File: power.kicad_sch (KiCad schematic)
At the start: 27 parts, among them P3 USB_C_Plug_USB2.0, P4 USB_C_Plug_USB2.0, SW2 SW_SPDT, U1 AMS1117-3.3

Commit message: fix at820 sym, impl audio pa
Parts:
- removed C8: 0.1uF, symbol Device:C
- removed C9: 10uF, symbol Device:C
- removed SW2: SW_SPDT, Button_Switch_SMD:Nidec_Copal_CAS-120A, symbol Switch:SW_SPDT
- added C15: 10uF, symbol Device:C
- added C16: 0.1uF, symbol Device:C
- added R21: 0R, symbol Device:R_US
- added SW3: SW_SPDT, Button_Switch_SMD:Nidec_Copal_CAS-120A, symbol Switch:SW_SPDT
- renumbered C25 to C13, C26 to C14, C11 to C17, C10 to C18, C12 to C19, C2 to C20, C13 to C21, C27 to C22, C14 to C23, C15 to C24, D3 to D1, D5 to D2, D6 to D3, P4 to P1, P3 to P2, R24 to R10, R11 to R4, R10 to R5, R20 to R6, R21 to R7, R22 to R8, R23 to R9, U1 to U3
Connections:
- net +3V3: now also SW3.3 (C)
- net AT_PMU_1V8: now also SW3.1 (A)
- net GND: now also C15.2, C16.2, R21.2
- new net AT_QSPI_VDD: C15.1, C16.1, SW3.2 (B)
- new net GNDA: R21.1

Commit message: sch features done, all drc passed
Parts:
- renumbered C13 to C15, C14 to C16, C15 to C18, C18 to C19, C16 to C20, C19 to C21, C20 to C22, C21 to C23, C22 to C24, C23 to C25, C24 to C26, R8 to R10, R9 to R11, R21 to R12, R10 to R13, R4 to R6, R5 to R7, R6 to R8, R7 to R9, SW3 to SW5
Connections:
- net at R7.2: now also P2.SH (SHIELD); no longer P2.S1 (SHIELD)
- net at R6.2: now also P1.SH (SHIELD); no longer P1.S1 (SHIELD)
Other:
- moved on the sheet: R12

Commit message: asigning footprint
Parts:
- removed P1, P2: USB_C_Plug_USB2.0, symbol Connector:USB_C_Plug_USB2.0
- added J8, J9: USB_C_Receptacle_USB2.0_16P, Connector_USB:USB_C_Receptacle_GCT_USB4105-xx-A_16P_TopMnt_Horizontal, symbol Connector:USB_C_Receptacle_USB2.0_16P
- C15, C16, C17, C18, C19, C20, C21, C22, C23, C24, C25, C26: footprint (none) -> Capacitor_SMD:C_0603_1608Metric_Pad1.08x0.95mm_HandSolder
- D1, D2: footprint Diode_SMD:D_SOD-323 -> Diode_SMD:D_SOD-323_HandSoldering
- D3: footprint (none) -> LED_SMD:LED_0603_1608Metric_Pad1.05x0.95mm_HandSolder
- FB1: value 90R/100M -> BLM18PG121SN1D; footprint (none) -> Inductor_SMD:L_0603_1608Metric_Pad1.05x0.95mm_HandSolder
- R10, R11: footprint Resistor_SMD:R_0603_1608Metric -> Resistor_SMD:R_0603_1608Metric_Pad0.98x0.95mm_HandSolder
- R12, R13, R6, R7: footprint (none) -> Resistor_SMD:R_0603_1608Metric_Pad0.98x0.95mm_HandSolder
- R8: renamed from R9; footprint Resistor_SMD:R_0603_1608Metric -> Resistor_SMD:R_0603_1608Metric_Pad0.98x0.95mm_HandSolder
- R9: renamed from R8; footprint Resistor_SMD:R_0603_1608Metric -> Resistor_SMD:R_0603_1608Metric_Pad0.98x0.95mm_HandSolder
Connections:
- net GND: now also J8.A1 (GND), J8.A12 (GND), J8.B1 (GND), J8.B12 (GND), J9.A1 (GND), J9.A12 (GND), J9.B1 (GND), J9.B12 (GND)
- net UART_USB_D+: now also J8.A6 (D+), J8.B6 (D+)
- net UART_USB_D-: now also J8.A7 (D-), J8.B7 (D-)
- net USB_D+: now also J9.A6 (D+), J9.B6 (D+)
- net USB_D-: now also J9.A7 (D-), J9.B7 (D-)
- net VBUS: now also J8.A4 (VBUS), J8.A9 (VBUS), J8.B4 (VBUS), J8.B9 (VBUS)
- net VBUS_B: now also J9.A4 (VBUS), J9.A9 (VBUS), J9.B4 (VBUS), J9.B9 (VBUS)
- net at R11.1: now also J8.A5 (CC1)
- net at R8.1: now also J8.B5 (CC2)
- net at R7.2: now also J9.SH (SHIELD)
- net at R9.1: now also J9.B5 (CC2)
- net at R10.1: now also J9.A5 (CC1)
- net at R6.2: now also J8.SH (SHIELD)
- no-connect marks 0 -> 4
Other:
- moved on the sheet: D1, R10, R9

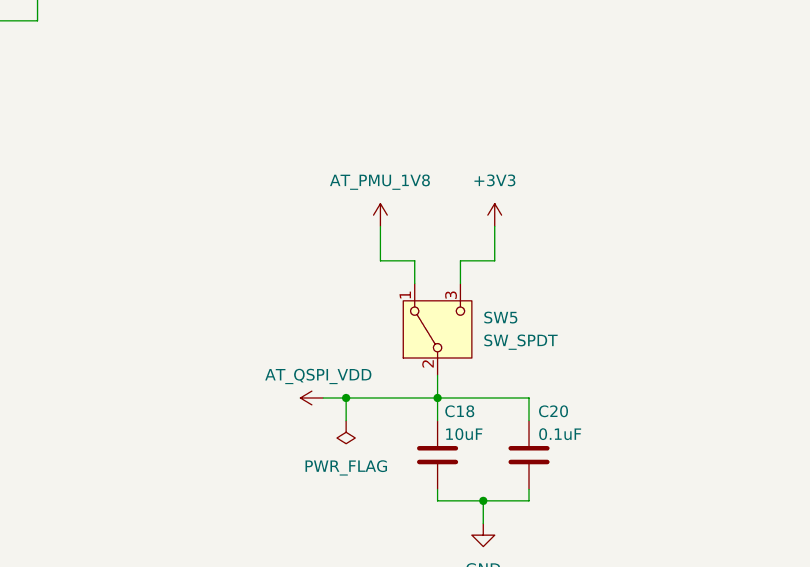
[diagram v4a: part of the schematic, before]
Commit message: refactor some switch circuit
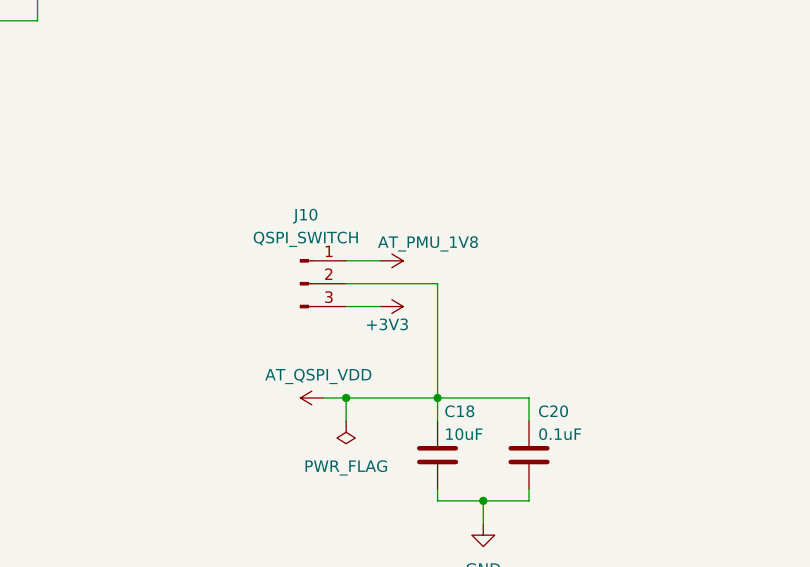
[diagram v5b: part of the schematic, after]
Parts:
- removed SW5: SW_SPDT, Button_Switch_SMD:Nidec_Copal_CAS-120A, symbol Switch:SW_SPDT
- added J10: QSPI_SWITCH, Connector_PinHeader_2.54mm:PinHeader_1x03_P2.54mm_Vertical, symbol Connector:Conn_01x03_Pin
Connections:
- net +3V3: now also J10.3 (Pin_3)
- net AT_PMU_1V8: now also J10.1 (Pin_1)
- net AT_QSPI_VDD: now also J10.2 (Pin_2)
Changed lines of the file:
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@@
 	(wire
 		(pts
-			(xy 153.67 91.44) (xy 153.67 95.25)
+			(xy 149.86 100.33) (xy 153.67 100.33)
 		)
 		(stroke
@@
 	(wire
 		(pts
-			(xy 153.67 95.25) (xy 157.48 95.25)
-		)
-		(stroke
-			(width 0)
-			(type default)
-		)
-	)
-	(wire
-		(pts
 			(xy 153.67 49.53) (xy 153.67 52.07)
 		)
@@
 	(wire
 		(pts
-			(xy 160.02 107.95) (xy 160.02 110.49)
-		)
-		(stroke
-			(width 0)
-			(type default)
-		)
-	)
-	(wire
-		(pts
 			(xy 73.66 137.16) (xy 73.66 154.94)
 		)
@@
 	(wire
 		(pts
-			(xy 157.48 95.25) (xy 157.48 97.79)
-		)
-		(stroke
-			(width 0)
-			(type default)
-		)
-	)
-	(wire
-		(pts
 			(xy 53.34 147.32) (xy 52.07 147.32)
 		)
@@
 	(wire
 		(pts
-			(xy 166.37 91.44) (xy 166.37 95.25)
-		)
-		(stroke
-			(width 0)
-			(type default)
-		)
-	)
-	(wire
-		(pts
-			(xy 166.37 95.25) (xy 162.56 95.25)
-		)
-		(stroke
-			(width 0)
-			(type default)
-		)
-	)
-	(wire
-		(pts
 			(xy 53.34 147.32) (xy 53.34 144.78)
 		)
@@
 	(wire
 		(pts
+			(xy 149.86 95.25) (xy 153.67 95.25)
+		)
+		(stroke
+			(width 0)
+			(type default)
+		)
+	)
+	(wire
+		(pts
 			(xy 194.31 52.07) (xy 194.31 49.53)
 		)
@@
 	(wire
 		(pts
-			(xy 115.57 68.58) (xy 105.41 68.58)
+			(xy 149.86 97.79) (xy 160.02 97.79)
 		)
 		(stroke
@@
 	(wire
 		(pts
-			(xy 170.18 110.49) (xy 170.18 113.03)
+			(xy 115.57 68.58) (xy 105.41 68.58)
 		)
 		(stroke
@@
 	(wire
 		(pts
-			(xy 64.77 171.45) (xy 64.77 167.64)
+			(xy 170.18 110.49) (xy 170.18 113.03)
 		)
 		(stroke
@@
 	(wire
 		(pts
-			(xy 27.94 77.47) (xy 27.94 78.74)
+			(xy 64.77 171.45) (xy 64.77 167.64)
 		)
 		(stroke
@@
 	(wire
 		(pts
-			(xy 50.8 39.37) (xy 59.69 39.37)
+			(xy 27.94 77.47) (xy 27.94 78.74)
 		)
 		(stroke
@@
 	(wire
 		(pts
-			(xy 64.77 68.58) (xy 74.93 68.58)
+			(xy 50.8 39.37) (xy 59.69 39.37)
 		)
 		(stroke
@@
 	(wire
 		(pts
-			(xy 162.56 95.25) (xy 162.56 97.79)
+			(xy 64.77 68.58) (xy 74.93 68.58)
 		)
 		(stroke
@@
 	(wire
 		(pts
+			(xy 160.02 97.79) (xy 160.02 110.49)
+		)
+		(stroke
+			(width 0)
+			(type default)
+		)
+	)
+	(wire
+		(pts
 			(xy 52.07 59.69) (xy 52.07 57.15)
 		)
@@
 	(symbol
 		(lib_id "power:+1V8")
-		(at 153.67 91.44 0)
+		(at 153.67 95.25 270)
 		(unit 1)
 		(body_style 1)
@@
 		(dnp no)
 		(property "Reference" "#PWR057"
-			(at 153.67 95.25 0)
+			(at 149.86 95.25 0)
 			(hide yes)
 			(show_name no)
@@
 		)
 		(property "Value" "AT_PMU_1V8"
-			(at 153.67 86.36 0)
+			(at 159.004 93.218 90)
 			(show_name no)
 			(do_not_autoplace no)
@@
 		)
 		(property "Footprint" ""
-			(at 153.67 91.44 0)
+			(at 153.67 95.25 0)
 			(hide yes)
 			(show_name no)
@@
 		)
 		(property "Datasheet" ""
-			(at 153.67 91.44 0)
+			(at 153.67 95.25 0)
 			(hide yes)
 			(show_name no)
@@
 		)
 		(property "Description" "Power symbol creates a global label with name \"+1V8\""
-			(at 153.67 91.44 0)
+			(at 153.67 95.25 0)
 			(hide yes)
 			(show_name no)
@@
 	)
 	(symbol
+		(lib_id "Connector:Conn_01x03_Pin")
+		(at 144.78 97.79 0)
+		(unit 1)
+		(body_style 1)
+		(exclude_from_sim no)
+		(in_bom yes)
+		(on_board yes)
+		(in_pos_files yes)
+		(dnp no)
+		(fields_autoplaced yes)
+		(property "Reference" "J10"
+			(at 145.415 90.17 0)
+			(show_name no)
+			(do_not_autoplace no)
+			(effects
+				(font
+					(size 1.27 1.27)
+				)
+			)
+		)
+		(property "Value" "QSPI_SWITCH"
+			(at 145.415 92.71 0)
+			(show_name no)
+			(do_not_autoplace no)
+			(effects
+				(font
+					(size 1.27 1.27)
+				)
+			)
+		)
+		(property "Footprint" "Connector_PinHeader_2.54mm:PinHeader_1x03_P2.54mm_Vertical"
+			(at 144.78 97.79 0)
+			(hide yes)
+			(show_name no)
+			(do_not_autoplace no)
+			(effects
+				(font
+					(size 1.27 1.27)
+				)
+			)
+		)
+		(property "Datasheet" ""
+			(at 144.78 97.79 0)
+			(hide yes)
+			(show_name no)
+			(do_not_autoplace no)
+			(effects
+				(font
+					(size 1.27 1.27)
+				)
+			)
+		)
+		(property "Description" "Generic connector, single row, 01x03, script generated"
+			(at 144.78 97.79 0)
+			(hide yes)
+			(show_name no)
+			(do_not_autoplace no)
+			(effects
+				(font
+					(size 1.27 1.27)
+				)
+			)
+		)
+		(pin "1"
+		)
+		(pin "2"
+		)
+		(pin "3"
+		)
+		(instances
+			(project "at820_picokit"
+				(path "/a8c0f85c-55b6-4da9-ba8c-71a36ed08e24/bdb32295-0012-48b2-b3aa-c4e9dc671aef"
+					(reference "J10")
+					(unit 1)
+				)
+			)
+		)
+	)
+	(symbol
 		(lib_id "Device:C")
 		(at 179.07 45.72 0)
@@
 	(symbol
 		(lib_id "power:+3V3")
-		(at 166.37 91.44 0)
+		(at 153.67 100.33 270)
 		(unit 1)
 		(body_style 1)
@@
 		(in_pos_files yes)
 		(dnp no)
-		(fields_autoplaced yes)
 		(property "Reference" "#PWR060"
-			(at 166.37 95.25 0)
+			(at 149.86 100.33 0)
 			(hide yes)
 			(show_name no)
@@
 		)
 		(property "Value" "+3V3"
-			(at 166.37 86.36 0)
+			(at 154.432 102.362 90)
 			(show_name no)
 			(do_not_autoplace no)
@@
 		)
 		(property "Footprint" ""
-			(at 166.37 91.44 0)
+			(at 153.67 100.33 0)
 			(hide yes)
 			(show_name no)
@@
 		)
 		(property "Datasheet" ""
-			(at 166.37 91.44 0)
+			(at 153.67 100.33 0)
 			(hide yes)
 			(show_name no)
@@
 		)
 		(property "Description" "Power symbol creates a global label with name \"+3V3\""
-			(at 166.37 91.44 0)
+			(at 153.67 100.33 0)
 			(hide yes)
 			(show_name no)
@@
 					(unit 1)
 				)
-			)
-		)
-	)
-	(symbol
-		(lib_id "Switch:SW_SPDT")
-		(at 160.02 102.87 90)
-		(unit 1)
-		(body_style 1)
-		(exclude_from_sim no)
-		(in_bom yes)
-		(on_board yes)
-		(in_pos_files yes)
-		(dnp no)
-		(fields_autoplaced yes)
-		(property "Reference" "SW5"
-			(at 165.1 101.5999 90)
-			(show_name no)
-			(do_not_autoplace no)
-			(effects
-				(font
-					(size 1.27 1.27)
-				)
-				(justify right)
-			)
-		)
-		(property "Value" "SW_SPDT"
-			(at 165.1 104.1399 90)
-			(show_name no)
-			(do_not_autoplace no)
-			(effects
-				(font
-					(size 1.27 1.27)
-				)
-				(justify right)
-			)
-		)
-		(property "Footprint" "Button_Switch_SMD:Nidec_Copal_CAS-120A"
-			(at 160.02 102.87 0)
-			(hide yes)
-			(show_name no)
-			(do_not_autoplace no)
-			(effects
-				(font
-					(size 1.27 1.27)
-				)
-			)
-		)
-		(property "Datasheet" ""
-			(at 167.64 102.87 0)
-			(hide yes)
-			(show_name no)
-			(do_not_autoplace no)
-			(effects
-				(font
-					(size 1.27 1.27)
-				)
-			)
-		)
-		(property "Description" "Switch, single pole double throw"
-			(at 160.02 102.87 0)
-			(hide yes)
-			(show_name no)
-			(do_not_autoplace no)
-			(effects
-				(font
-					(size 1.27 1.27)
-				)
-			)
-		)
-		(pin "3"
-		)
-		(pin "1"
-		)
-		(pin "2"
-		)
-		(instances
-			(project "at820_picokit"
-				(path "/a8c0f85c-55b6-4da9-ba8c-71a36ed08e24/bdb32295-0012-48b2-b3aa-c4e9dc671aef"
-					(reference "SW5")
-					(unit 1)
-				)

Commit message: sch all done, footprint done
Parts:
- renumbered R9 to R10, R10 to R11, R11 to R12, R12 to R13, R13 to R14, R6 to R7, R7 to R8, R8 to R9, U3 to U4

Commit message: components loc done, pcb ing
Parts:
- added H1, H2, H3, H4: MountingHole_Pad, MountingHole:MountingHole_3.2mm_M3_Pad, symbol Mechanical:MountingHole_Pad
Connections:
- net GND: now also H1.1, H2.1, H3.1, H4.1
